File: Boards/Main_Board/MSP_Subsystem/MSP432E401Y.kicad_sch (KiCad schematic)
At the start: 4 parts, among them J1-J3 Conn_01x10, J4-J2 Conn_01x10, J5-J7 Conn_01x10, J8-J6 Conn_01x10

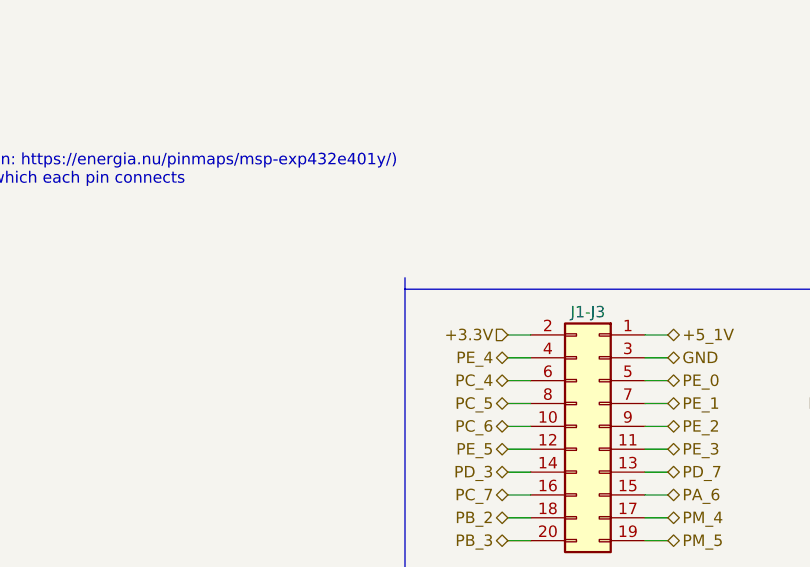
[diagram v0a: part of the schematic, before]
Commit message: Correct spacing on sensor board, refactor datasheets and project libraries
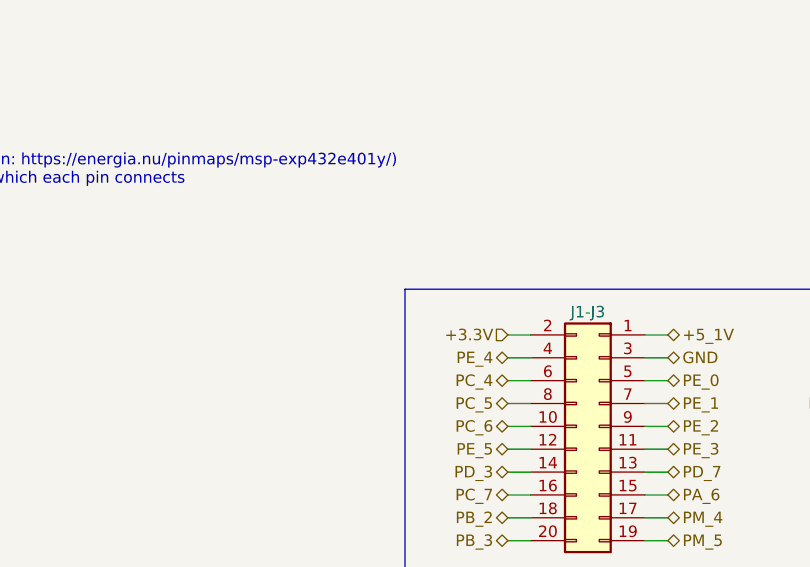
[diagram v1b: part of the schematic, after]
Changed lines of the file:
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@@
-    (stroke (width 0) (type default) (color 0 0 0 0))
-  )
-  (polyline (pts (xy 109.22 55.88) (xy 109.22 54.61))
     (stroke (width 0) (type default) (color 0 0 0 0))
   )

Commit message: Fix typos
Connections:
- net PA_6 renamed PD_6
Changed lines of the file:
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@@
     (effects (font (size 1.27 1.27)) (justify left))
   )
-  (hierarchical_label "PA_6" (shape bidirectional) (at 138.43 78.74 0)
+  (hierarchical_label "PD_6" (shape bidirectional) (at 138.43 78.74 0)
     (effects (font (size 1.27 1.27)) (justify left))
   )
